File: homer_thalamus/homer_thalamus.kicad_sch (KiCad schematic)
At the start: 17 parts, among them J1 GPIO, J2 Mot_Drive_Conn, J3 Right_Motor_Conn, J4 Left_Motor_Conn, SW1 SW_PULLDOWN, U1 DRV8874_CARRIER_RIGHT, U2 DRV8874_CARRIER_LEFT, U3 HC-SR04

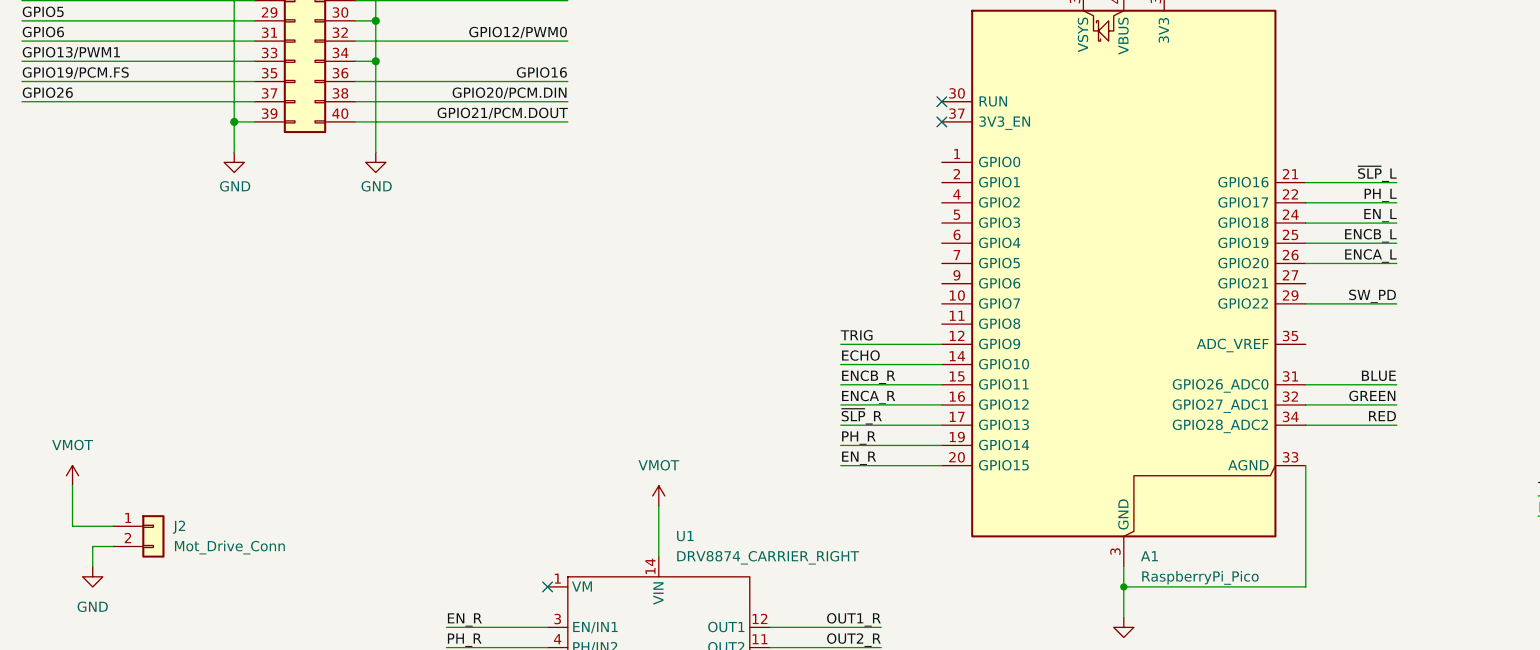
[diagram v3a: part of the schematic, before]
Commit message: add gy-521 to schematic
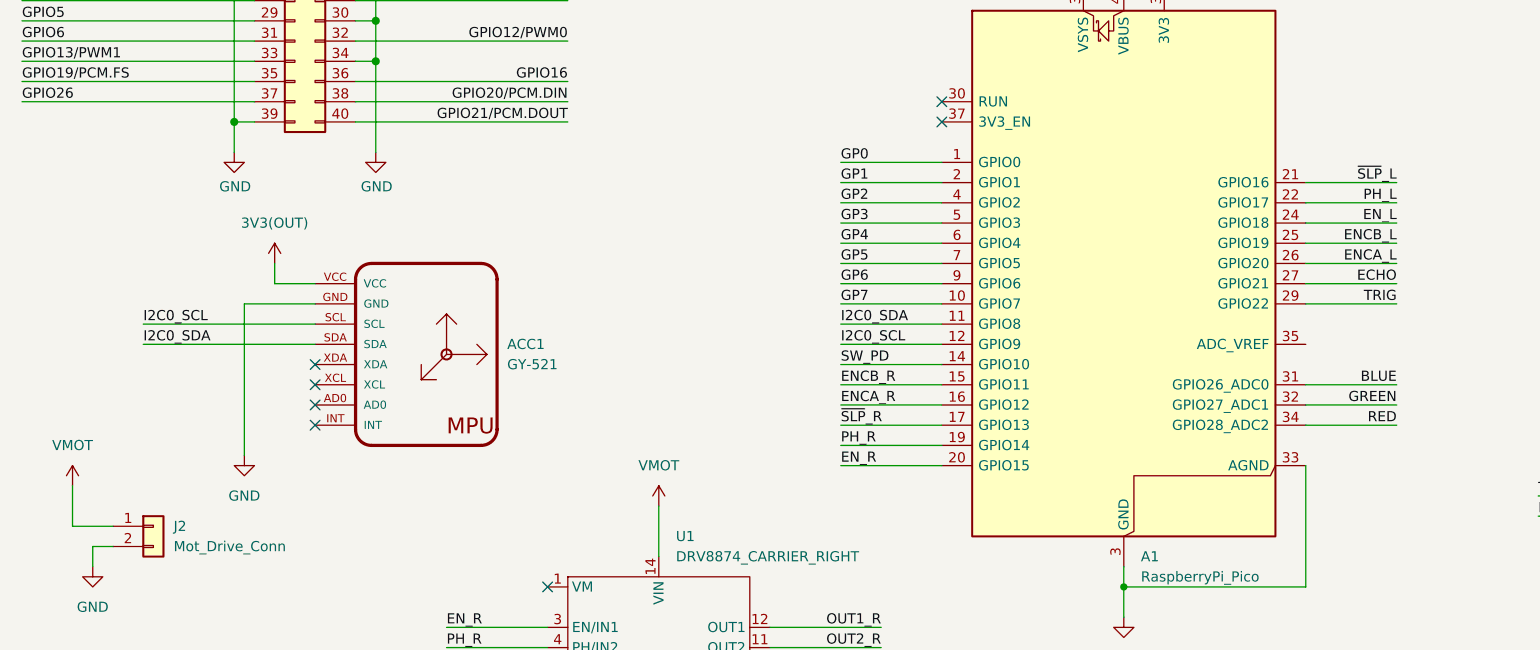
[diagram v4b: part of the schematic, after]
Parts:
- added ACC1: GY-521, symbol GY-521:GY-521
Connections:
- net 3V3(OUT): now also ACC1.VCC
- net ECHO: now also A1.27 (GPIO21); no longer A1.14 (GPIO10)
- net GND: now also ACC1.GND
- net SW_PD: now also A1.14 (GPIO10); no longer A1.29 (GPIO22)
- net TRIG: now also A1.29 (GPIO22); no longer A1.12 (GPIO9)
- net GP0: now reaches A1.1 (GPIO0)
- net GP7: now reaches A1.10 (GPIO7)
- net I2C0_SDA: now reaches A1.11 (GPIO8)
- net I2C0_SDA: now also ACC1.SDA
- net GP1: now reaches A1.2 (GPIO1)
- net GP2: now reaches A1.4 (GPIO2)
- net GP3: now reaches A1.5 (GPIO3)
- net GP4: now reaches A1.6 (GPIO4)
- net GP5: now reaches A1.7 (GPIO5)
- net GP6: now reaches A1.9 (GPIO6)
- new net I2C0_SCL: A1.12 (GPIO9), ACC1.SCL
- no-connect marks 12 -> 16

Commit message: finish up schematic v0
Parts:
- added J5: Spare_GP_Conn, symbol Connector:Conn_01x10_Pin
- added J6: VBUS_Conn, symbol Connector_Generic:Conn_02x02_Counter_Clockwise
- J2: value Mot_Drive_Conn -> MotDrv_Pow_Conn
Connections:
- net GND: now also J5.3 (Pin_3), J5.8 (Pin_8), J6.3 (Pin_3), J6.4 (Pin_4)
- net GP0: now also J5.10 (Pin_10)
- net GP1: now also J5.9 (Pin_9)
- net GP2: now also J5.7 (Pin_7)
- net GP3: now also J5.6 (Pin_6)
- net GP4: now also J5.5 (Pin_5)
- net GP5: now also J5.4 (Pin_4)
- net GP6: now also J5.2 (Pin_2)
- net GP7: now also J5.1 (Pin_1)
- net VBUS: now also J6.1 (Pin_1), J6.2 (Pin_2)
- net VSYS: no longer names the net of A1.39 (VSYS)
- no-connect marks 16 -> 17

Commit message: assign footprints
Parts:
- ACC1: footprint (none) -> GY-521:GY-521
- C1: footprint (none) -> Capacitor_THT:C_Disc_D4.7mm_W2.5mm_P5.00mm
- D1: footprint (none) -> LED_THT:LED_D5.0mm-4_RGB_Wide_Pins
- J2: footprint (none) -> Connector_JST:JST_XH_B2B-XH-AM_1x02_P2.50mm_Vertical
- J3, J4: footprint (none) -> Connector_PinHeader_2.54mm:PinHeader_1x06_P2.54mm_Vertical
- J5: footprint (none) -> Connector_PinHeader_2.54mm:PinHeader_1x10_P2.54mm_Vertical
- J6: footprint (none) -> Connector_PinHeader_2.54mm:PinHeader_2x02_P2.54mm_Vertical
- R1, R2, R3, R4, R5, R6: footprint (none) -> Resistor_THT:R_Axial_DIN0207_L6.3mm_D2.5mm_P7.62mm_Horizontal
- SW1: footprint (none) -> Button_Switch_THT:SW_PUSH_6mm
- U1, U2: footprint (none) -> DRV8874_Carrier:DRV8874_Carrier
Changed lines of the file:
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@@
 			)
 		)
-		(property "Footprint" ""
+		(property "Footprint" "LED_THT:LED_D5.0mm-4_RGB_Wide_Pins"
 			(at 227.33 81.28 0)
 			(effects
@@
 			)
 		)
-		(property "Footprint" ""
+		(property "Footprint" "Resistor_THT:R_Axial_DIN0207_L6.3mm_D2.5mm_P7.62mm_Horizontal"
 			(at 242.57 81.788 90)
 			(effects
@@
 			)
 		)
-		(property "Footprint" ""
+		(property "Footprint" "Connector_PinHeader_2.54mm:PinHeader_1x06_P2.54mm_Vertical"
 			(at 127 176.53 0)
 			(effects
@@
 			)
 		)
-		(property "Footprint" ""
+		(property "Footprint" "DRV8874_Carrier:DRV8874_Carrier"
 			(at 39.37 161.29 0)
 			(effects
@@
 			)
 		)
-		(property "Footprint" ""
+		(property "Footprint" "Resistor_THT:R_Axial_DIN0207_L6.3mm_D2.5mm_P7.62mm_Horizontal"
 			(at 226.06 121.412 90)
 			(effects
@@
 			)
 		)
-		(property "Footprint" ""
+		(property "Footprint" "Connector_PinHeader_2.54mm:PinHeader_1x06_P2.54mm_Vertical"
 			(at 88.9 176.53 0)
 			(effects
@@
 			)
 		)
-		(property "Footprint" ""
+		(property "Footprint" "Resistor_THT:R_Axial_DIN0207_L6.3mm_D2.5mm_P7.62mm_Horizontal"
 			(at 236.982 43.18 90)
 			(effects
@@
 			)
 		)
-		(property "Footprint" ""
+		(property "Footprint" "Resistor_THT:R_Axial_DIN0207_L6.3mm_D2.5mm_P7.62mm_Horizontal"
 			(at 242.57 86.868 90)
 			(effects
@@
 			)
 		)
-		(property "Footprint" ""
+		(property "Footprint" "Capacitor_THT:C_Disc_D4.7mm_W2.5mm_P5.00mm"
 			(at 229.5652 46.99 0)
 			(effects
@@
 			)
 		)
-		(property "Footprint" ""
+		(property "Footprint" "Connector_PinHeader_2.54mm:PinHeader_1x10_P2.54mm_Vertical"
 			(at 205.74 35.56 0)
 			(effects
@@
 			)
 		)
-		(property "Footprint" ""
+		(property "Footprint" "Resistor_THT:R_Axial_DIN0207_L6.3mm_D2.5mm_P7.62mm_Horizontal"
 			(at 242.57 76.708 90)
 			(effects
@@
 			)
 		)
-		(property "Footprint" ""
+		(property "Footprint" "Button_Switch_THT:SW_PUSH_6mm"
 			(at 233.68 30.48 0)
 			(effects
@@
 			)
 		)
-		(property "Footprint" ""
+		(property "Footprint" "Connector_PinHeader_2.54mm:PinHeader_2x02_P2.54mm_Vertical"
 			(at 166.37 24.13 0)
 			(effects
@@
 			)
 		)
-		(property "Footprint" ""
+		(property "Footprint" "Resistor_THT:R_Axial_DIN0207_L6.3mm_D2.5mm_P7.62mm_Horizontal"
 			(at 235.458 133.35 90)
 			(effects
@@
 			)
 		)
-		(property "Footprint" ""
+		(property "Footprint" "DRV8874_Carrier:DRV8874_Carrier"
 			(at 96.52 139.7 0)
 			(effects
@@
 			)
 		)
-		(property "Footprint" ""
+		(property "Footprint" "Connector_JST:JST_XH_B2B-XH-AM_1x02_P2.50mm_Vertical"
 			(at 38.1 124.46 0)
 			(effects
@@
 			)
 		)
-		(property "Footprint" ""
+		(property "Footprint" "GY-521:GY-521"
 			(at 74.93 102.87 0)
 			(effects

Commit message: update pcb layout
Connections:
- net ENCA_L: now also J4.6 (Pin_6); no longer J4.5 (Pin_5)
- net ENCB_L: now also J4.5 (Pin_5); no longer J4.6 (Pin_6)
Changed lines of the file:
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@@
 	)
 	(label "ENCB_L"
-		(at 146.05 184.15 180)
+		(at 146.05 181.61 180)
 		(effects
 			(font
@@
 	)
 	(label "ENCA_L"
-		(at 146.05 181.61 180)
+		(at 146.05 184.15 180)
 		(effects
 			(font

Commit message: update pcb layout
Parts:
- J2: footprint Connector_JST:JST_XH_B2B-XH-AM_1x02_P2.50mm_Vertical -> Connector_JST:JST_XH_B2B-XH-A_1x02_P2.50mm_Vertical
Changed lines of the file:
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@@
 			)
 		)
-		(property "Footprint" "Connector_JST:JST_XH_B2B-XH-AM_1x02_P2.50mm_Vertical"
+		(property "Footprint" "Connector_JST:JST_XH_B2B-XH-A_1x02_P2.50mm_Vertical"
 			(at 38.1 124.46 0)
 			(effects
